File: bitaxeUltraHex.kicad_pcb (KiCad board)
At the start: 4 copper layers, 84.5 x 129.5 mm, 336 parts, among them J1 Conn_01x01, J2 Conn_01x01, J3 TC2030-IDC, J4 USB_C_Receptacle_USB2.0, J5 Conn_01x04, J6 Conn_01x04, Q1 NTMFS5C673NLT1G, Q2 CSD17577Q5A, Q3 NTMFS5C673NLT1G, Q4 CSD17577Q5A, Q5 BSS123, SW1 GT-TC029B-H025-L1N, SW2 GT-TC029B-H025-L1N, U1 uA7805, U10 TMP1075, U11 TMP1075, U12 EMC2302, U13 BM1366_mode1, U14 ADP171AUJ-R7, U15 ADP171AUJ-R7, U16 BM1366_mode1, U17 25MHz, U18 TLV3544, U19 BM1366_mode0, U2 RT9080-33GJ5, U20 ADP171AUJ-R7, U21 ADP171AUJ-R7, U22 BM1366_mode0, U23 TLV3544, U24 BM1366_mode1, U25 ADP171AUJ-R7, U26 ADP171AUJ-R7, U27 BM1366_mode1, U3 INA219AIDCNR, U4 TPS40305, U5 MIC5504, U6 DS4432U+, U7 SN74AVC4T774, U8 176x320_st7789, U9 ESP32-S3-WROOM-1, Y1 32.768kHz

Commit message: more parts placement
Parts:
- removed the R73 at (74.4, 91.2)
- removed the R74 at (76.7, 91.7)
- removed the R77 at (88.8, 91.0)
- D1, R18, R19, R34, R35, R62, R68, R98, R99: moved to B.Cu
- U19, U22: value BM1366_mode0 -> BM1366_mode1
- moved R35 62.5 mm to (100.6, 140.7), turned to 90 degrees
- moved R34 59.2 mm to (96.0, 140.7), turned to 90 degrees
- moved C101 57.3 mm to (64.8, 147.3), turned to 0 degrees
- moved C67 53.6 mm to (115.6, 147.1), turned to -90 degrees
- moved C105 52.7 mm to (66.8, 147.1), turned to 0 degrees
- moved C99 51.0 mm to (69.4, 147.6), turned to 0 degrees
- moved C69 50.6 mm to (114.6, 148.1), turned to -90 degrees
- moved C71 49.4 mm to (115.6, 149.4), turned to -90 degrees
- moved C97 47.0 mm to (71.6, 146.3), turned to 0 degrees
- moved C73 46.0 mm to (114.6, 150.6), turned to -90 degrees
- moved R68 41.7 mm to (89.9, 140.7), turned to -90 degrees
- moved R62 40.8 mm to (85.3, 140.7), turned to -90 degrees
- moved TP31 37.6 mm to (71.9, 163.8)
- moved TP32 37.6 mm to (74.7, 164.3)
- moved R76 37.2 mm to (81.3, 146.8), turned to 180 degrees
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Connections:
- net /BM1366-1/TEMP_N1 renamed /BM1366-1/TEMP_N1_1
- net /BM1366-1/TEMP_N2 renamed /BM1366-1/TEMP_N2_1
- net /BM1366-1/TEMP_P1 renamed /BM1366-1/TEMP_P1_1
- net /BM1366-1/TEMP_P2 renamed /BM1366-1/TEMP_P2_1
- net /BM1366-2/CLKO renamed /BM1366-3/CLKI3
- net /BM1366-2/TEMP_N1 renamed /BM1366-2/TEMP_N1_2
- net /BM1366-2/TEMP_N2 renamed /BM1366-2/TEMP_N2_2
- net /BM1366-2/TEMP_P1 renamed /BM1366-2/TEMP_P1_2
- net /BM1366-2/TEMP_P2 renamed /BM1366-2/TEMP_P2_2
- net /BM1366-3/BO renamed /BM1366-3/BO3
- net /BM1366-3/CLKO renamed /BM1366-3/CLKO3
- net /BM1366-3/CO renamed /BM1366-3/CO3
- net /BM1366-3/NRSTO renamed /BM1366-3/NRSTO3
- net /BM1366-3/RI renamed /BM1366-3/RI3
- net /BM1366-3/TEMP_N1 renamed /BM1366-3/TEMP_N1_3
- net /BM1366-3/TEMP_N2 renamed /BM1366-3/TEMP_N2_3
- net /BM1366-3/TEMP_P1 renamed /BM1366-3/TEMP_P1_3
- net /BM1366-3/TEMP_P2 renamed /BM1366-3/TEMP_P2_3
- net Net-(U13-BI) renamed /BM1366-1/BI1
- C104 pad 2: Net-(U22-MODE_0) -> Net-(U22-MODE_1)
- C111 pad 2: /BM1366-3/CI -> /BM1366-3/CI3
- C117 pad 2: /BM1366-3/NRSTI -> /BM1366-3/NRSTI3
- C127 pad 2: /BM1366-3/BI -> /BM1366-3/BI3
- C72 pad 2: /BM1366-2/CI -> /BM1366-2/CI2
- C80 pad 2: /BM1366-2/NRSTI -> /BM1366-2/NRSTI2
- C82 pad 1: Net-(U19-MODE_0) -> Net-(U19-MODE_1)
- C87 pad 1: Net-(U19-MODE_0) -> Net-(U19-MODE_1)
- C88 pad 2: /BM1366-2/BI -> /BM1366-2/BI2
- C91 pad 2: /BM1366-1/VDD1 -> GND
- C93 pad 2: /BM1366-1/VDD1 -> GND
- C94 pad 2: /BM1366-1/VDD1 -> GND
- C95 pad 2: /BM1366-1/VDD1 -> GND
- C98 pad 2: /BM1366-1/VDD1 -> GND
- R102 pad 1: /BM1366-3/BI -> /BM1366-3/BI3
- R103 pad 2: /BM1366-2/VDD2 -> /BM1366-3/GND
- R105 pad 1: /BM1366-3/RO -> /BM1366-3/RO3
- R108 pad 1: /BM1366-3/RO -> /BM1366-2/RI
- R36 pad 2: /BM1366-2/NRSTI -> /BM1366-1/NRSTO
- R37 pad 2: /BM1366-2/CI -> /BM1366-1/CO
- R39 pad 2: /BM1366-2/BI -> /BM1366-1/BO
- R40 pad 2: /BM1366-1/CLKO -> /BM1366-2/CLKI2
- R41 pad 2: /BM1366-2/RO -> /BM1366-1/RI
- R42 pad 1: Net-(U19-RI) (its old number) -> Net-(U22-RI)
- R42 pad 2: /BM1366-3/RO -> /BM1366-2/RI
- R43 pad 1: Net-(U19-NRSTO) (its old number) -> Net-(U22-NRSTO)
- R43 pad 2: /BM1366-3/NRSTI -> /BM1366-2/NRSTO
- R44 pad 2: /BM1366-1/VDD1 -> GND
- R46 pad 1: /BM1366-2/CI -> /BM1366-1/CO
- R47 pad 1: Net-(U19-CLKO) (its old number) -> Net-(U22-CLKO)
- R48 pad 1: Net-(U19-BO) (its old number) -> Net-(U22-BO)
- R48 pad 2: /BM1366-3/BI -> /BM1366-2/BO
- R49 pad 1: Net-(U19-CO) (its old number) -> Net-(U22-CO)
- R49 pad 2: /BM1366-3/CI -> /BM1366-2/CO
- R50 pad 1: /BM1366-2/CI -> /BM1366-2/CI2
- R51 pad 2: /BM1366-1/VDD1 -> GND
- R53 pad 1: /BM1366-2/NRSTI -> /BM1366-1/NRSTO
- R58 pad 2: Net-(U19-MODE_0) -> Net-(U19-MODE_1)
- R59 pad 1: /BM1366-2/NRSTI -> /BM1366-2/NRSTI2
- R63 pad 2: /BM1366-1/VDD1 -> GND
- R65 pad 1: /BM1366-2/BI -> /BM1366-1/BO
- R71 pad 1: /BM1366-2/BI -> /BM1366-2/BI2
- R72 pad 2: /BM1366-1/VDD1 -> GND
- R74 pad 1: /BM1366-2/RO -> /BM1366-2/RO2
- R76 pad 1: Net-(U22-MODE_0) -> Net-(U22-MODE_1)
- R77 pad 1: /BM1366-2/RO -> /BM1366-1/RI
- R78 pad 2: /BM1366-2/VDD2 -> /BM1366-3/GND
- R80 pad 1: /BM1366-3/CI -> /BM1366-2/CO
- R81 pad 1: /BM1366-3/CI -> /BM1366-3/CI3
- R82 pad 2: /BM1366-2/VDD2 -> /BM1366-3/GND
- R84 pad 1: /BM1366-3/NRSTI -> /BM1366-2/NRSTO
- R88 pad 1: /BM1366-3/NRSTI -> /BM1366-3/NRSTI3
- R93 pad 2: /BM1366-2/VDD2 -> /BM1366-3/GND
- R95 pad 1: /BM1366-3/BI -> /BM1366-2/BO
- U13 pad 8: /BM1366-1/CLKI -> /BM1366-1/CLKI1
- U18 pad 1: /BM1366-2/CI -> /BM1366-2/CI2
- U18 pad 7: /BM1366-2/NRSTI -> /BM1366-2/NRSTI2
- U18 pad 8: /BM1366-2/BI -> /BM1366-2/BI2
- U19 pad 17: unconnected-(U19-MODE_1-Pad17) -> Net-(U19-MODE_1)
- U19 pad 18: Net-(U19-MODE_0) -> unconnected-(U19-MODE_0-Pad18)
- U19 pad 5: Net-(U19-CO) (its old number) -> /BM1366-2/NRSTI2
- U19 pad 6: Net-(U19-CLKO) (its old number) -> /BM1366-2/BI2
- U19 pad 7: Net-(U19-RI) (its old number) -> /BM1366-2/RO2
- U19 pad 8: Net-(U19-BO) (its old number) -> /BM1366-2/CLKI2
- U19 pad 9: Net-(U19-NRSTO) (its old number) -> /BM1366-2/CI2
- U22 pad 12: Net-(U19-MODE_0) -> Net-(U19-MODE_1)
- U22 pad 17: unconnected-(U22-MODE_1-Pad17) -> Net-(U22-MODE_1)
- U22 pad 18: Net-(U22-MODE_0) -> unconnected-(U22-MODE_0-Pad18)
- U22 pad 20: /BM1366-2/NRSTI -> Net-(U22-CO)
- U22 pad 21: /BM1366-2/BI -> Net-(U22-CLKO)
- U22 pad 22: /BM1366-2/RO -> Net-(U22-RI)
- U22 pad 23: /BM1366-1/CLKO -> Net-(U22-BO)
- U22 pad 24: /BM1366-2/CI -> Net-(U22-NRSTO)
- U23 pad 1: /BM1366-3/CI -> /BM1366-3/CI3
- U23 pad 7: /BM1366-3/NRSTI -> /BM1366-3/NRSTI3
- U23 pad 8: /BM1366-3/BI -> /BM1366-3/BI3
- U24 pad 5: /BM1366-3/NRSTI -> /BM1366-3/NRSTI3
- U24 pad 6: /BM1366-3/BI -> /BM1366-3/BI3
- U24 pad 7: /BM1366-3/RO -> /BM1366-3/RO3
- U24 pad 9: /BM1366-3/CI -> /BM1366-3/CI3
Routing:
- net /BM1366-2/VDD2: vias 0 -> 18
- net /BM1366-1/VDD1: vias 0 -> 18
- added copper zone on F.Cu, net /BM1366-1/VDD1
- added copper zone on In1.Cu, net /BM1366-1/VDD1
- added copper zone on F.Cu, net /BM1366-2/VDD2
- added copper zone on In1.Cu, net /BM1366-2/VDD2
- removed copper zone on In1.Cu, net (none)
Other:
- board text added: "C129"
- board text added: "C134"

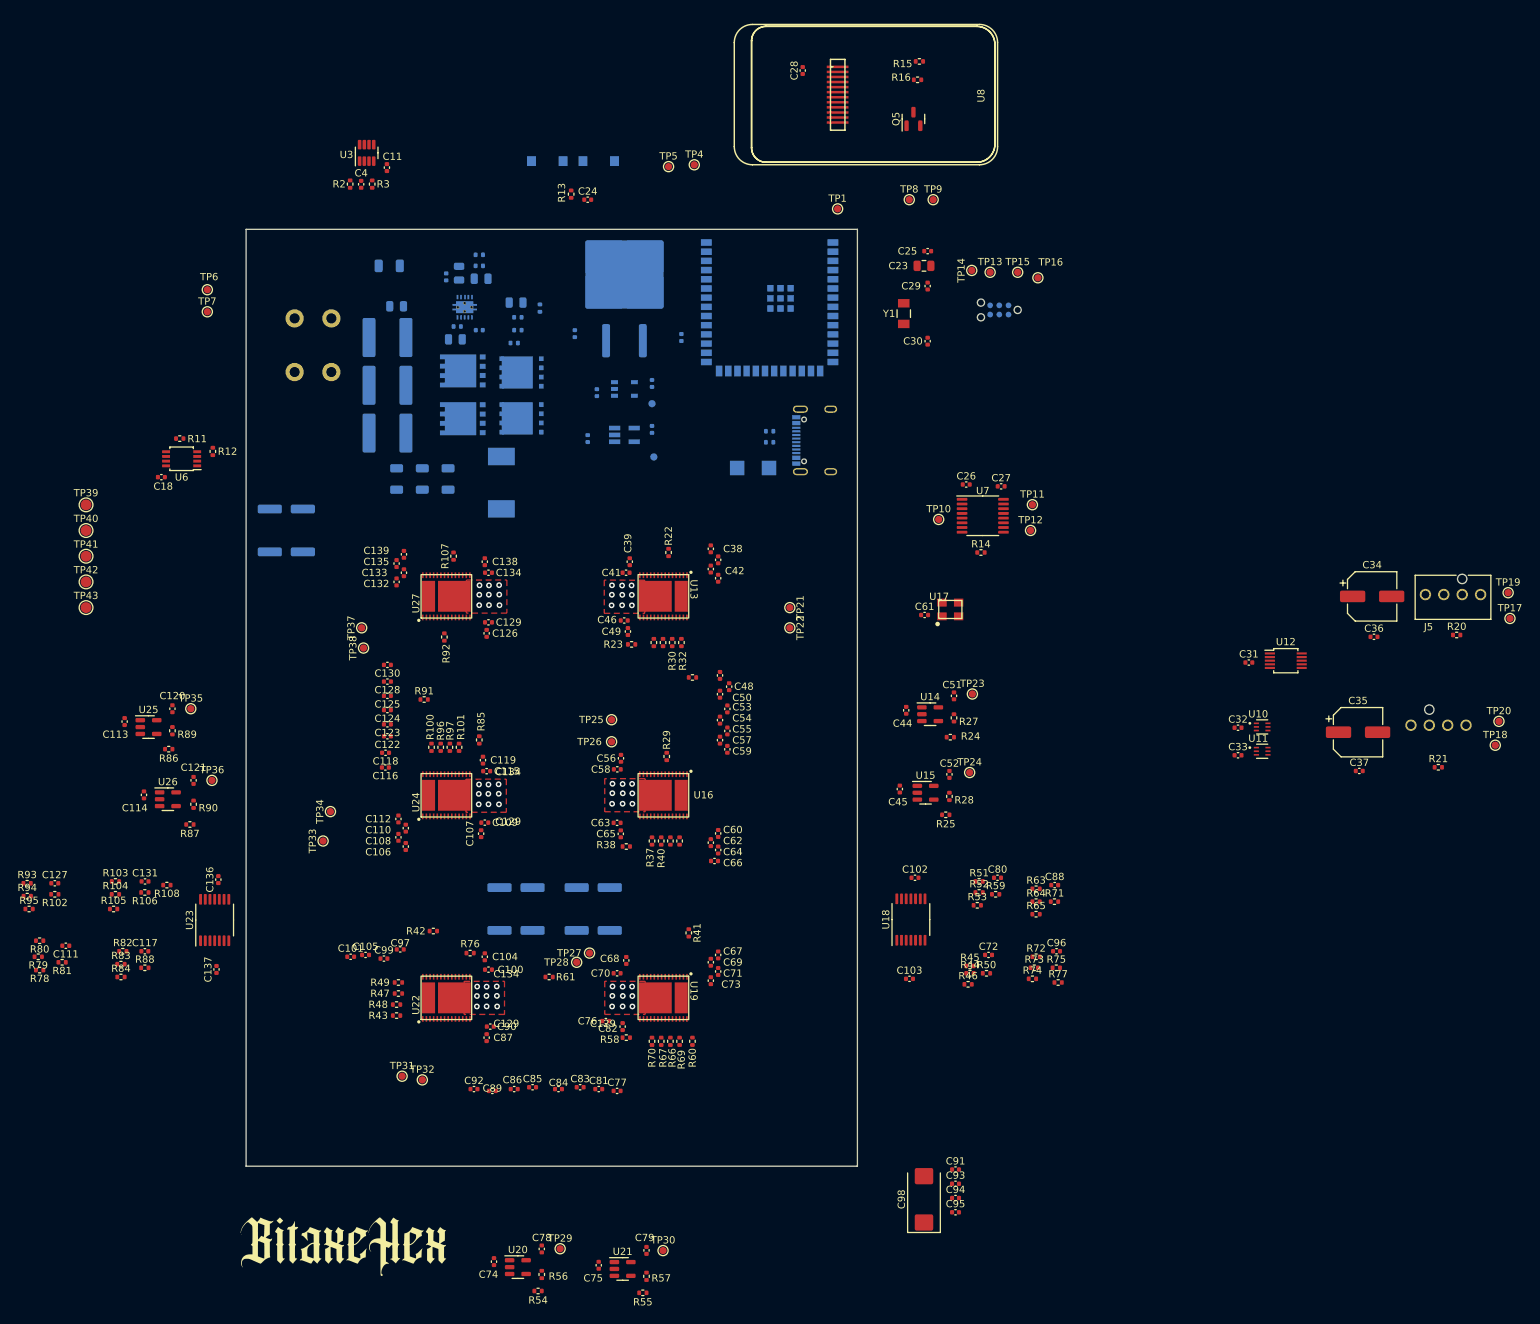
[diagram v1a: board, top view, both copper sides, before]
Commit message: switch power/comms topology to columns and zig-zag
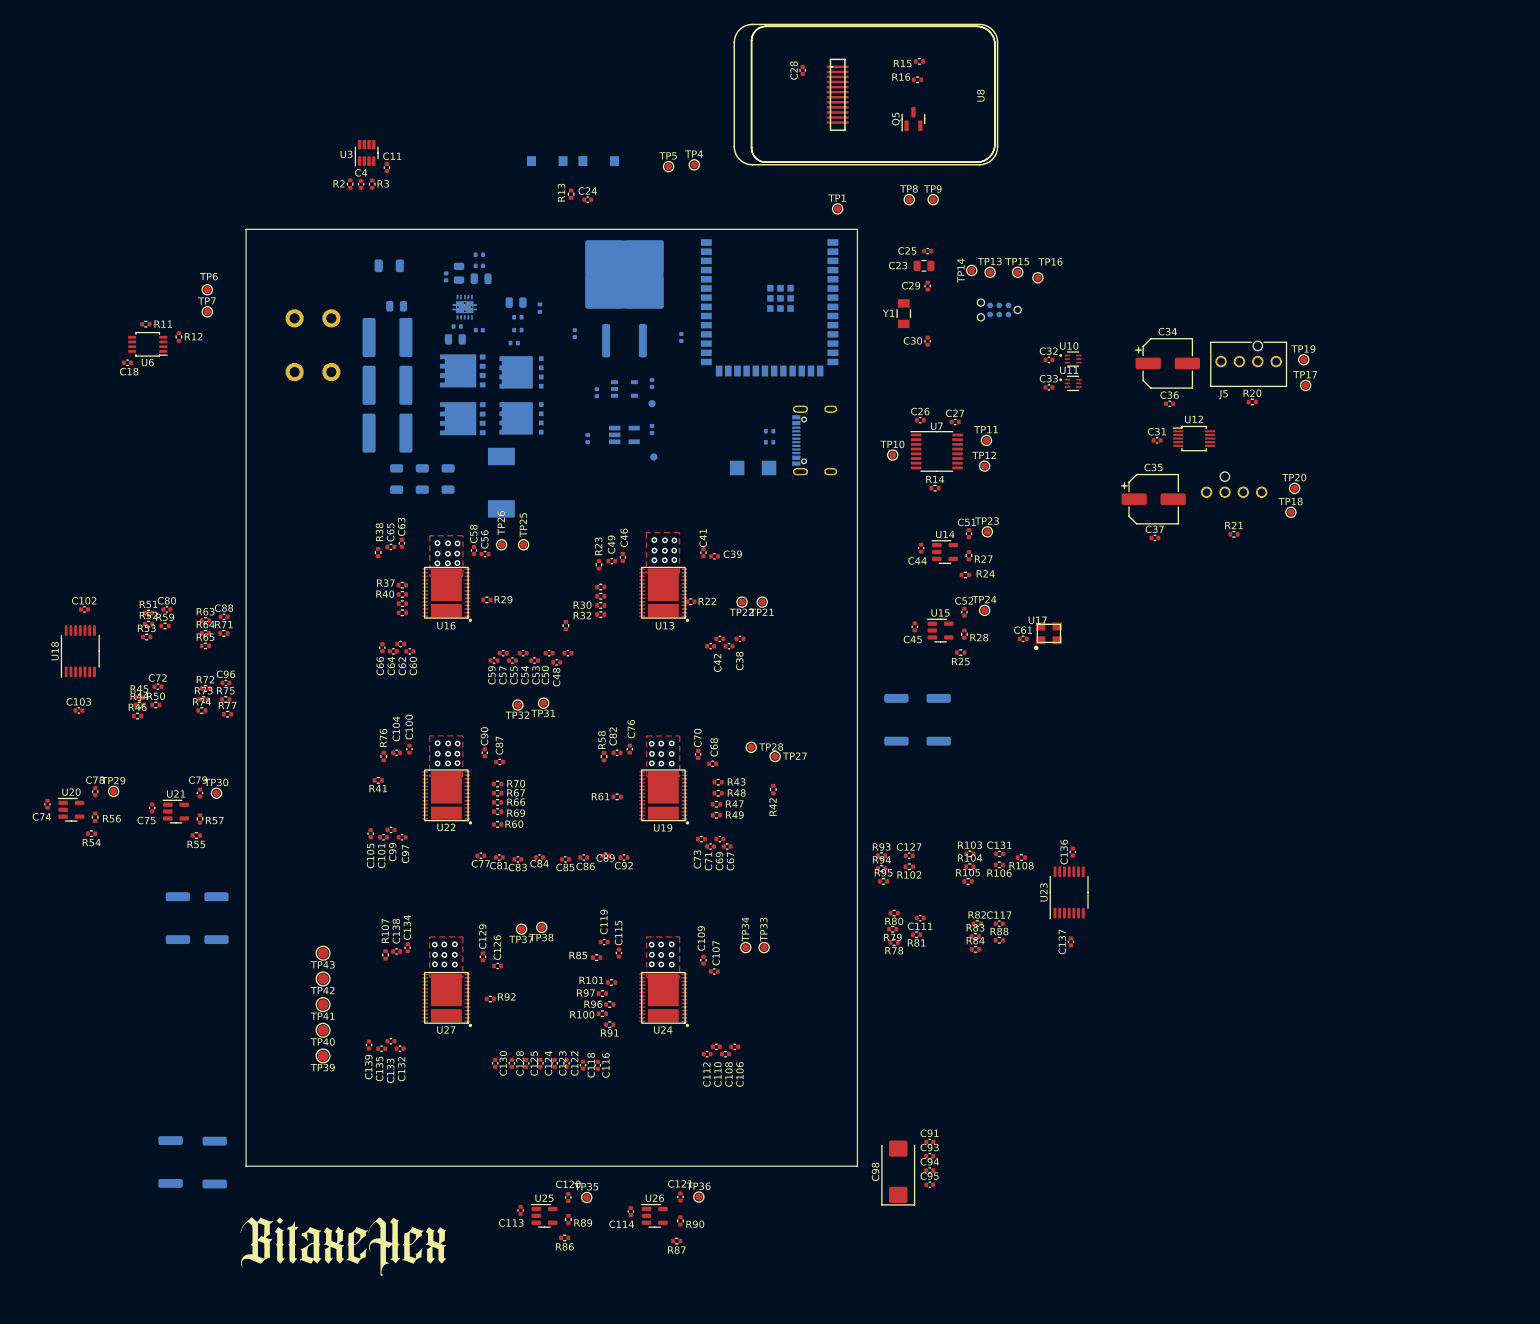
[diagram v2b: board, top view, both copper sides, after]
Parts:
- U19: renamed from U22; value BM1366_mode1 -> BM1366_mode0
- U22: renamed from U19; value BM1366_mode1 -> BM1366_mode0
- moved R77 120.6 mm to (47.8, 113.8)
- moved C102 120.6 mm to (28.0, 99.3)
- moved C103 120.6 mm to (27.2, 113.3)
- moved R44 120.6 mm to (35.6, 112.5)
- moved R45 120.6 mm to (35.6, 111.5)
- moved R50 120.6 mm to (37.8, 112.5)
- moved R63 120.6 mm to (44.7, 100.8)
- moved R72 120.6 mm to (44.7, 110.2)
- moved U18 120.6 mm to (27.4, 105.1)
- moved C72 120.6 mm to (38.1, 110.0)
- moved C80 120.6 mm to (39.4, 99.3)
- moved C88 120.6 mm to (47.3, 100.3)
- moved C96 120.6 mm to (47.5, 109.5)
- moved R46 120.6 mm to (35.3, 114.0)
- moved R51 120.6 mm to (36.8, 99.8)
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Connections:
- C105 pad 2: Net-(C105-Pad2) -> Net-(U22-VDD4_1)
- C67 pad 1: Net-(C67-Pad1) -> Net-(U19-VDD4_0)
- C84 pad 2: Net-(C84-Pad2) -> Net-(U19-VDD4_1)
- C85 pad 1: Net-(C84-Pad2) -> Net-(U19-VDD4_1)
- R42 pad 1: Net-(U22-RI) -> Net-(U19-RI)
- R43 pad 1: Net-(U22-NRSTO) -> Net-(U19-NRSTO)
- R47 pad 1: Net-(U22-CLKO) -> Net-(U19-CLKO)
- R48 pad 1: Net-(U22-BO) -> Net-(U19-BO)
- R49 pad 1: Net-(U22-CO) -> Net-(U19-CO)
- R58 pad 1: Net-(U19-NC) -> Net-(U19-MODE_0)
- R60 pad 1: Net-(C84-Pad2) -> Net-(U19-VDD4_1)
- R60 pad 2: Net-(U19-NRSTO) -> Net-(U19-CI)
- R61 pad 1: Net-(U19-RI) -> Net-(U19-RO)
- R61 pad 2: Net-(U22-RO) -> Net-(U22-RI)
- R66 pad 1: Net-(U19-BO) -> Net-(U19-CLKI)
- R66 pad 2: Net-(U22-BI) -> Net-(U22-CLKO)
- R67 pad 1: Net-(U19-CLKO) -> Net-(U19-BI)
- R67 pad 2: Net-(U22-CLKI) -> Net-(U22-BO)
- R69 pad 1: Net-(U19-NRSTO) -> Net-(U19-CI)
- R69 pad 2: Net-(U22-NRSTI) -> Net-(U22-CO)
- R70 pad 1: Net-(U19-CO) -> Net-(U19-NRSTI)
- R70 pad 2: Net-(U22-CI) -> Net-(U22-NRSTO)
- R76 pad 2: Net-(U22-NC) -> Net-(U22-MODE_0)
- U19 pad 1: Net-(U19-VDD1_1) -> Net-(U19-VDD1_0)
- U19 pad 10: /BM1366-2/TEMP_P2_2 -> /BM1366-2/TEMP_P1_2
- U19 pad 11: /BM1366-2/TEMP_N2_2 -> /BM1366-2/TEMP_N1_2
- U19 pad 12: Net-(U19-MODE_1) -> Net-(U19-MODEO)
- U19 pad 17: Net-(U22-MODE_1) -> Net-(U19-MODE_1)
- U19 pad 18: unconnected-(U22-MODE_0-Pad18) -> Net-(U19-MODE_0)
- U19 pad 19: Net-(U22-NC) -> unconnected-(U19-NC-Pad19)
- U19 pad 2: Net-(U19-VDD2_1) -> Net-(U19-VDD2_0)
- U19 pad 20: Net-(U22-CO) -> Net-(U19-NRSTI)
- U19 pad 21: Net-(U22-CLKO) -> Net-(U19-BI)
- U19 pad 22: Net-(U22-RI) -> Net-(U19-RO)
- U19 pad 23: Net-(U22-BO) -> Net-(U19-CLKI)
- U19 pad 24: Net-(U22-NRSTO) -> Net-(U19-CI)
- U19 pad 25: Net-(C105-Pad2) -> Net-(U19-VDD4_1)
- U19 pad 26: Net-(U22-VDD3_1) -> Net-(U19-VDD3_1)
- U19 pad 27: Net-(U22-VDD2_1) -> Net-(U19-VDD2_1)
- U19 pad 28: Net-(U22-VDD1_1) -> Net-(U19-VDD1_1)
- U19 pad 3: Net-(U19-VDD3_1) -> Net-(U19-VDD3_0)
- U19 pad 4: Net-(C84-Pad2) -> Net-(U19-VDD4_0)
- U19 pad 5: Net-(U22-NRSTI) -> Net-(U19-CO)
- U19 pad 6: Net-(U22-BI) -> Net-(U19-CLKO)
- U19 pad 7: Net-(U22-RO) -> Net-(U19-RI)
- U19 pad 8: Net-(U22-CLKI) -> Net-(U19-BO)
- U19 pad 9: Net-(U22-CI) -> Net-(U19-NRSTO)
- U22 pad 1: Net-(U19-VDD1_0) -> Net-(U19-VDD1_1)
- U22 pad 10: /BM1366-2/TEMP_P1_2 -> /BM1366-2/TEMP_P2_2
- U22 pad 11: /BM1366-2/TEMP_N1_2 -> /BM1366-2/TEMP_N2_2
- U22 pad 12: Net-(U19-MODEO) -> Net-(U19-MODE_1)
- U22 pad 17: Net-(U19-MODE_1) -> Net-(U22-MODE_1)
- U22 pad 18: unconnected-(U19-MODE_0-Pad18) -> Net-(U22-MODE_0)
- U22 pad 19: Net-(U19-NC) -> unconnected-(U22-NC-Pad19)
- U22 pad 2: Net-(U19-VDD2_0) -> Net-(U19-VDD2_1)
- U22 pad 20: Net-(U19-CO) -> /BM1366-2/NRSTI2
- U22 pad 21: Net-(U19-CLKO) -> /BM1366-2/BI2
- U22 pad 22: Net-(U19-RI) -> /BM1366-2/RO2
- U22 pad 23: Net-(U19-BO) -> /BM1366-2/CLKI2
- U22 pad 24: Net-(U19-NRSTO) -> /BM1366-2/CI2
- U22 pad 25: Net-(C84-Pad2) -> Net-(U22-VDD4_1)
- U22 pad 26: Net-(U19-VDD3_1) -> Net-(U22-VDD3_1)
- U22 pad 27: Net-(U19-VDD2_1) -> Net-(U22-VDD2_1)
- U22 pad 28: Net-(U19-VDD1_1) -> Net-(U22-VDD1_1)
- U22 pad 3: Net-(U19-VDD3_0) -> Net-(U19-VDD3_1)
- U22 pad 4: Net-(C67-Pad1) -> Net-(U19-VDD4_1)
- U22 pad 5: /BM1366-2/NRSTI2 -> Net-(U22-CO)
- U22 pad 6: /BM1366-2/BI2 -> Net-(U22-CLKO)
- U22 pad 7: /BM1366-2/RO2 -> Net-(U22-RI)
- U22 pad 8: /BM1366-2/CLKI2 -> Net-(U22-BO)
- U22 pad 9: /BM1366-2/CI2 -> Net-(U22-NRSTO)
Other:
- board text removed: "C129"
- board text removed: "C134"

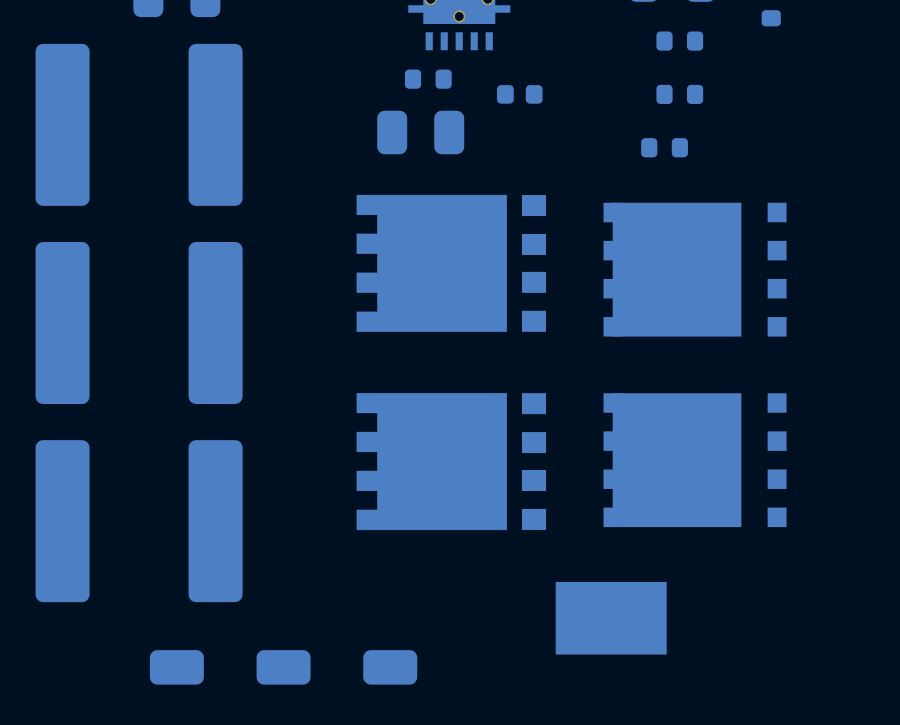
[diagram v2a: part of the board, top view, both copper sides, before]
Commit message: fixed part numbers and footprints on the buck reg FETs
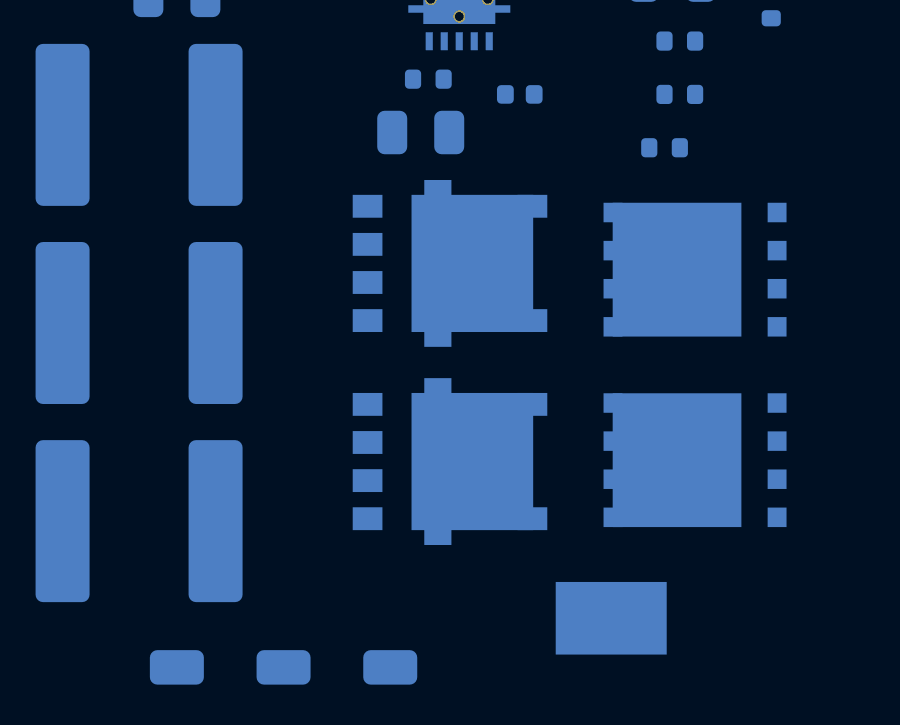
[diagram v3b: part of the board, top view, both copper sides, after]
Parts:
- Q1, Q3: footprint bitaxe:CSD17311Q5 -> bitaxe:NTMFS5C673NLT1G
